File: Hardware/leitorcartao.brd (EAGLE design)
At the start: 34.5 x 56.7 mm, 154 parts, among them IC1 TL084, IC2 TL084, Q1 DMN3404, Q4 BC847ALT1SMD, Q5 BC847ALT1SMD, Q6 BC847ALT1SMD, Q7 BC847ALT1SMD, Q8 MMBT4403, Q9 MMBT4401, U1 SAMD20E14A-AUT, U3 TLV1117-50CDCYR, U4 MFRC52202HN1, U5 LP2985-33DBVR, X1 ANTENA 125kHz, X2 MIFARE ANTENA

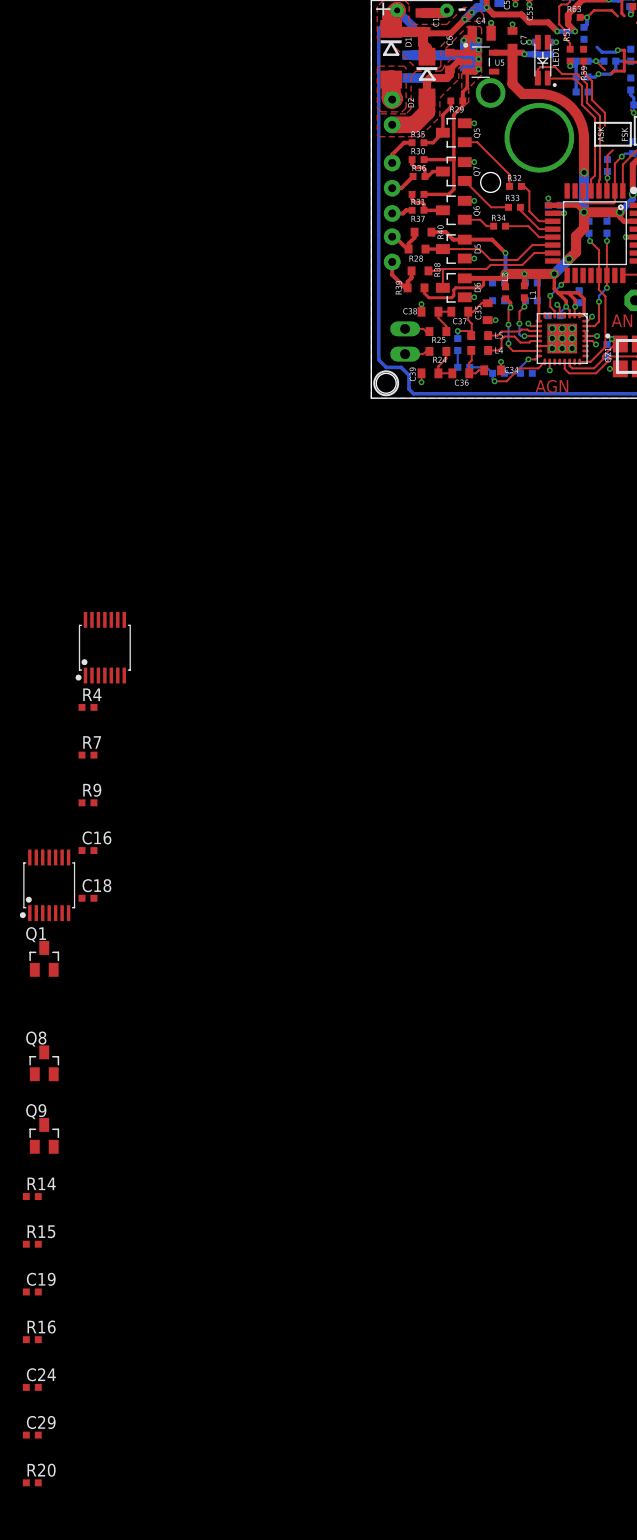
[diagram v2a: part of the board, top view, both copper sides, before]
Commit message: Finalização do esquema do RFID, falta valores de PSK e FSK.
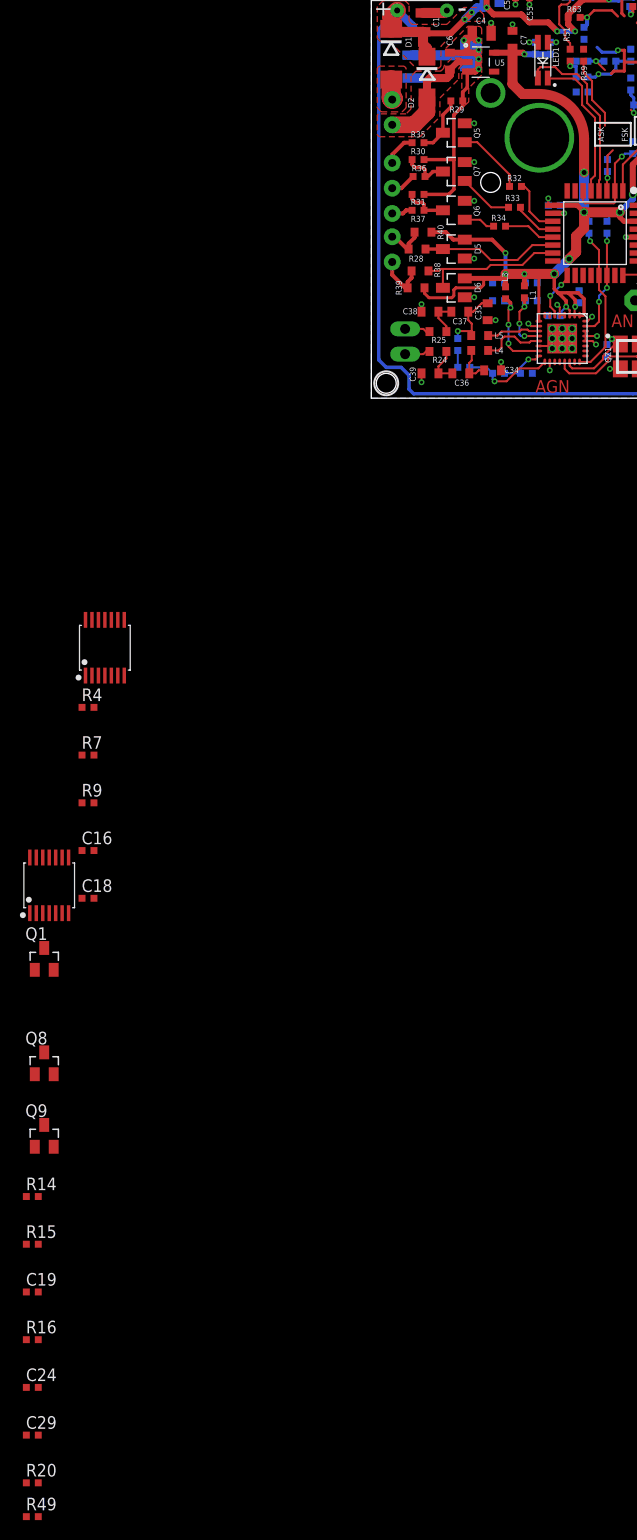
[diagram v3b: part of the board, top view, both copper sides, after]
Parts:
- added R49: F:P:5.1k, RFiD:R0402
- C24: value (none) -> F:C:100p
- C29, C48, C50: value (none) -> F:P:68p
- C47, C51: value (none) -> F:P:100p
- R14: value (none) -> 470k
- R15: value (none) -> 100
- R16, R51, R54: value (none) -> F:P:5.6k
- R20: value (none) -> C:P:270k
- R52, R55: value (none) -> F:P:5.1k
- R53, R56: value (none) -> F:P:270k
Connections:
- net GND: now also R49.1
- net N$29: now also R49.2
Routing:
- net N$28: track 4.20 -> 1.70 mm
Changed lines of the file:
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@@
 <attribute name="VALUE" x="23.805" y="42.165" size="1" layer="27" rot="R90"/>
 </element>
-<element name="R51" library="RFiD" package="R0402" value="" x="20" y="34.5" smashed="yes" rot="R270">
+<element name="R51" library="RFiD" package="R0402" value="F:P:5.6k" x="20" y="34.5" smashed="yes" rot="R270">
 <attribute name="CUSTOMER_PN" value="R/1k/5%/04" x="20" y="34.5" size="1.778" layer="27" rot="R270" display="off"/>
 <attribute name="NAME" x="19.335" y="37.335" size="0.6096" layer="25" font="vector" ratio="11" rot="R270"/>
 <attribute name="VALUE" x="18.095" y="35.135" size="1" layer="27" rot="R270"/>
 </element>
-<element name="R52" library="RFiD" package="R0402" value="" x="21.2" y="30.8" smashed="yes" rot="MR0">
+<element name="R52" library="RFiD" package="R0402" value="F:P:5.1k" x="21.2" y="30.8" smashed="yes" rot="MR0">
 <attribute name="CUSTOMER_PN" value="R/1k/5%/04" x="21.2" y="30.8" size="1.778" layer="28" rot="MR0" display="off"/>
 <attribute name="NAME" x="22.035" y="29.635" size="0.6096" layer="26" font="vector" ratio="11" rot="MR0"/>
 <attribute name="VALUE" x="21.835" y="28.895" size="1" layer="28" rot="MR0"/>
 </element>
-<element name="C47" library="RFiD" package="C0402" value="" x="21.2" y="33.9" smashed="yes" rot="MR0">
+<element name="C47" library="RFiD" package="C0402" value="F:P:100p" x="21.2" y="33.9" smashed="yes" rot="MR0">
 <attribute name="CUSTOMER_PN" value="C/1n/100V/C04" x="21.2" y="33.9" size="1.778" layer="28" rot="MR0" display="off"/>
 <attribute name="NAME" x="21.835" y="34.435" size="0.6096" layer="26" font="vector" ratio="11" rot="MR0"/>
 <attribute name="VALUE" x="21.835" y="31.995" size="1" layer="28" rot="MR0"/>
 </element>
-<element name="C48" library="RFiD" package="C0402" value="" x="21.2" y="32.3" smashed="yes" rot="MR0">
+<element name="C48" library="RFiD" package="C0402" value="F:P:68p" x="21.2" y="32.3" smashed="yes" rot="MR0">
 <attribute name="CUSTOMER_PN" value="C/1n/100V/C04" x="21.2" y="32.3" size="1.778" layer="28" rot="MR0" display="off"/>
 <attribute name="NAME" x="20.035" y="32.035" size="0.6096" layer="26" font="vector" ratio="11" rot="MR0"/>
 <attribute name="VALUE" x="21.835" y="30.395" size="1" layer="28" rot="MR0"/>
 </element>
-<element name="R53" library="RFiD" package="R0402" value="" x="24" y="33.9" smashed="yes" rot="MR180">
+<element name="R53" library="RFiD" package="R0402" value="F:P:270k" x="24" y="33.9" smashed="yes" rot="MR180">
 <attribute name="CUSTOMER_PN" value="R/1k/5%/04" x="24" y="33.9" size="1.778" layer="28" rot="MR180" display="off"/>
 <attribute name="NAME" x="23.165" y="33.265" size="0.6096" layer="26" font="vector" ratio="11" rot="MR180"/>
 <attribute name="VALUE" x="23.365" y="35.805" size="1" layer="28" rot="MR180"/>
 </element>
-<element name="R54" library="RFiD" package="R0402" value="" x="27.8" y="34.5" smashed="yes" rot="MR90">
+<element name="R54" library="RFiD" package="R0402" value="F:P:5.6k" x="27.8" y="34.5" smashed="yes" rot="MR90">
 <attribute name="CUSTOMER_PN" value="R/1k/5%/04" x="27.8" y="34.5" size="1.778" layer="28" rot="MR90" display="off"/>
 <attribute name="NAME" x="28.335" y="35.265" size="0.6096" layer="26" font="vector" ratio="11" rot="MR90"/>
@@
 <attribute name="VALUE" x="24.195" y="33.865" size="1" layer="28" rot="MR90"/>
 </element>
-<element name="R55" library="RFiD" package="R0402" value="" x="29.4" y="32.8" smashed="yes" rot="MR270">
+<element name="R55" library="RFiD" package="R0402" value="F:P:5.1k" x="29.4" y="32.8" smashed="yes" rot="MR270">
 <attribute name="CUSTOMER_PN" value="R/1k/5%/04" x="29.4" y="32.8" size="1.778" layer="28" rot="MR270" display="off"/>
 <attribute name="NAME" x="29.665" y="31.835" size="0.6096" layer="26" font="vector" ratio="11" rot="MR270"/>
 <attribute name="VALUE" x="31.305" y="33.435" size="1" layer="28" rot="MR270"/>
 </element>
-<element name="C50" library="RFiD" package="C0402" value="" x="27.8" y="31.6" smashed="yes" rot="MR90">
+<element name="C50" library="RFiD" package="C0402" value="F:P:68p" x="27.8" y="31.6" smashed="yes" rot="MR90">
 <attribute name="CUSTOMER_PN" value="C/1n/100V/C04" x="27.8" y="31.6" size="1.778" layer="28" rot="MR90" display="off"/>
 <attribute name="NAME" x="28.635" y="32.735" size="0.6096" layer="26" font="vector" ratio="11" rot="MR0"/>
 <attribute name="VALUE" x="25.895" y="30.965" size="1" layer="28" rot="MR90"/>
 </element>
-<element name="C51" library="RFiD" package="C0402" value="" x="26.1" y="31.6" smashed="yes" rot="MR90">
+<element name="C51" library="RFiD" package="C0402" value="F:P:100p" x="26.1" y="31.6" smashed="yes" rot="MR90">
 <attribute name="CUSTOMER_PN" value="C/1n/100V/C04" x="26.1" y="31.6" size="1.778" layer="28" rot="MR90" display="off"/>
 <attribute name="NAME" x="24.935" y="30.765" size="0.6096" layer="26" font="vector" ratio="11" rot="MR90"/>
 <attribute name="VALUE" x="24.195" y="30.965" size="1" layer="28" rot="MR90"/>
 </element>
-<element name="R56" library="RFiD" package="R0402" value="" x="27" y="29.5" smashed="yes" rot="MR0">
+<element name="R56" library="RFiD" package="R0402" value="F:P:270k" x="27" y="29.5" smashed="yes" rot="MR0">
 <attribute name="CUSTOMER_PN" value="R/1k/5%/04" x="27" y="29.5" size="1.778" layer="28" rot="MR0" display="off"/>
 <attribute name="NAME" x="28.765" y="30.335" size="0.6096" layer="26" font="vector" ratio="11" rot="MR270"/>
@@
 <element name="Q8" library="RFiD" package="SOT23" value="MMBT4403" x="-32.9" y="-66.9"/>
 <element name="Q9" library="RFiD" package="SOT23" value="MMBT4401" x="-32.9" y="-74.2"/>
-<element name="R14" library="RFiD" package="R0402" value="" x="-34.1" y="-80.3">
+<element name="R14" library="RFiD" package="R0402" value="470k" x="-34.1" y="-80.3">
 <attribute name="CUSTOMER_PN" value="R/1M/5%/04" x="-34.1" y="-80.3" size="1.778" layer="27" display="off"/>
 </element>
-<element name="R15" library="RFiD" package="R0402" value="" x="-34.1" y="-85.1">
+<element name="R15" library="RFiD" package="R0402" value="100" x="-34.1" y="-85.1">
 <attribute name="CUSTOMER_PN" value="R/1M/5%/04" x="-34.1" y="-85.1" size="1.778" layer="27" display="off"/>
 </element>
@@
 <attribute name="CUSTOMER_PN" value="C/1n/100V/C04" x="-34.1" y="-89.9" size="1.778" layer="27" display="off"/>
 </element>
-<element name="R16" library="RFiD" package="R0402" value="" x="-34.1" y="-94.7">
+<element name="R16" library="RFiD" package="R0402" value="F:P:5.6k" x="-34.1" y="-94.7">
 <attribute name="CUSTOMER_PN" value="R/1k/5%/04" x="-34.1" y="-94.7" size="1.778" layer="27" display="off"/>
 </element>
-<element name="C24" library="RFiD" package="C0402" value="" x="-34.1" y="-99.5">
+<element name="C24" library="RFiD" package="C0402" value="F:C:100p" x="-34.1" y="-99.5">
 <attribute name="CUSTOMER_PN" value="C/1n/100V/C04" x="-34.1" y="-99.5" size="1.778" layer="27" display="off"/>
 </element>
-<element name="C29" library="RFiD" package="C0402" value="" x="-34.1" y="-104.3">
+<element name="C29" library="RFiD" package="C0402" value="F:P:68p" x="-34.1" y="-104.3">
 <attribute name="CUSTOMER_PN" value="C/1n/100V/C04" x="-34.1" y="-104.3" size="1.778" layer="27" display="off"/>
 </element>
-<element name="R20" library="RFiD" package="R0402" value="" x="-34.1" y="-109.1">
+<element name="R20" library="RFiD" package="R0402" value="C:P:270k" x="-34.1" y="-109.1">
 <attribute name="CUSTOMER_PN" value="R/1k/5%/04" x="-34.1" y="-109.1" size="1.778" layer="27" display="off"/>
+</element>
+<element name="R49" library="RFiD" package="R0402" value="F:P:5.1k" x="-34.1" y="-112.5">
+<attribute name="CUSTOMER_PN" value="R/1k/5%/04" x="-34.1" y="-112.5" size="1.778" layer="27" display="off"/>
 </element>
 </elements>
@@
 <contactref element="IC1" pad="11"/>
 <contactref element="IC2" pad="11"/>
+<contactref element="R49" pad="1"/>
+<wire x1="-32.9" y1="-65.8" x2="-34.7" y2="-112.5" width="0" layer="19" extent="1-1"/>
 <wire x1="-31.95" y1="-57.5" x2="-32.9" y2="-65.8" width="0" layer="19" extent="1-1"/>
 <wire x1="-32.4" y1="-46.2" x2="-31.95" y2="-57.5" width="0" layer="19" extent="1-1"/>
@@
 <wire x1="20" y1="35.7" x2="20" y2="35.1" width="0.2032" layer="1"/>
 </signal>
-<signal name="N$70">
-<contactref element="R51" pad="2"/>
-<contactref element="C47" pad="2"/>
-<contactref element="R52" pad="2"/>
-<contactref element="C48" pad="2"/>
-<wire x1="20.6" y1="30.8" x2="20.6" y2="32.3" width="0.3048" layer="16"/>
-<wire x1="20.6" y1="32.3" x2="20.6" y2="33.4" width="0.3048" layer="16"/>
-<wire x1="20.6" y1="33.4" x2="20.6" y2="33.9" width="0.3048" layer="16"/>
-<via x="20" y="33.4" extent="1-16" drill="0.3"/>
-<wire x1="20" y1="33.4" x2="20" y2="33.9" width="0.2032" layer="1"/>
-<wire x1="20.6" y1="33.4" x2="20" y2="33.4" width="0.3048" layer="16"/>
-</signal>
 <signal name="N$71">
 <contactref element="C48" pad="1"/>
@@
 <contactref element="C24" pad="2"/>
 <contactref element="R16" pad="2"/>
+<contactref element="R49" pad="2"/>
+<wire x1="-33.5" y1="-104.3" x2="-33.5" y2="-112.5" width="0" layer="19" extent="1-1"/>
 <wire x1="-33.5" y1="-99.5" x2="-33.5" y2="-104.3" width="0" layer="19" extent="1-1"/>
 <wire x1="-33.5" y1="-94.7" x2="-33.5" y2="-99.5" width="0" layer="19" extent="1-1"/>
@@
 <wire x1="-24.85" y1="-22.3" x2="17.6" y2="40.4" width="0" layer="19" extent="1-16"/>
 </signal>
+<signal name="N$28">
+<contactref element="R51" pad="2"/>
+<contactref element="C47" pad="2"/>
+<contactref element="R52" pad="2"/>
+<contactref element="C48" pad="2"/>
+<wire x1="20.6" y1="32.3" x2="20.6" y2="33.4" width="0.3048" layer="16"/>
+<via x="20" y="33.4" extent="1-16" drill="0.3"/>
+<wire x1="20.6" y1="33.4" x2="20" y2="33.4" width="0.3048" layer="16"/>
+<wire x1="20.6" y1="33.4" x2="20.6" y2="33.9" width="0" layer="19" extent="16-16"/>
+<wire x1="20" y1="33.9" x2="20" y2="33.4" width="0" layer="19" extent="1-1"/>
+<wire x1="20.6" y1="30.8" x2="20.6" y2="32.3" width="0" layer="19" extent="16-16"/>
+</signal>
 </signals>

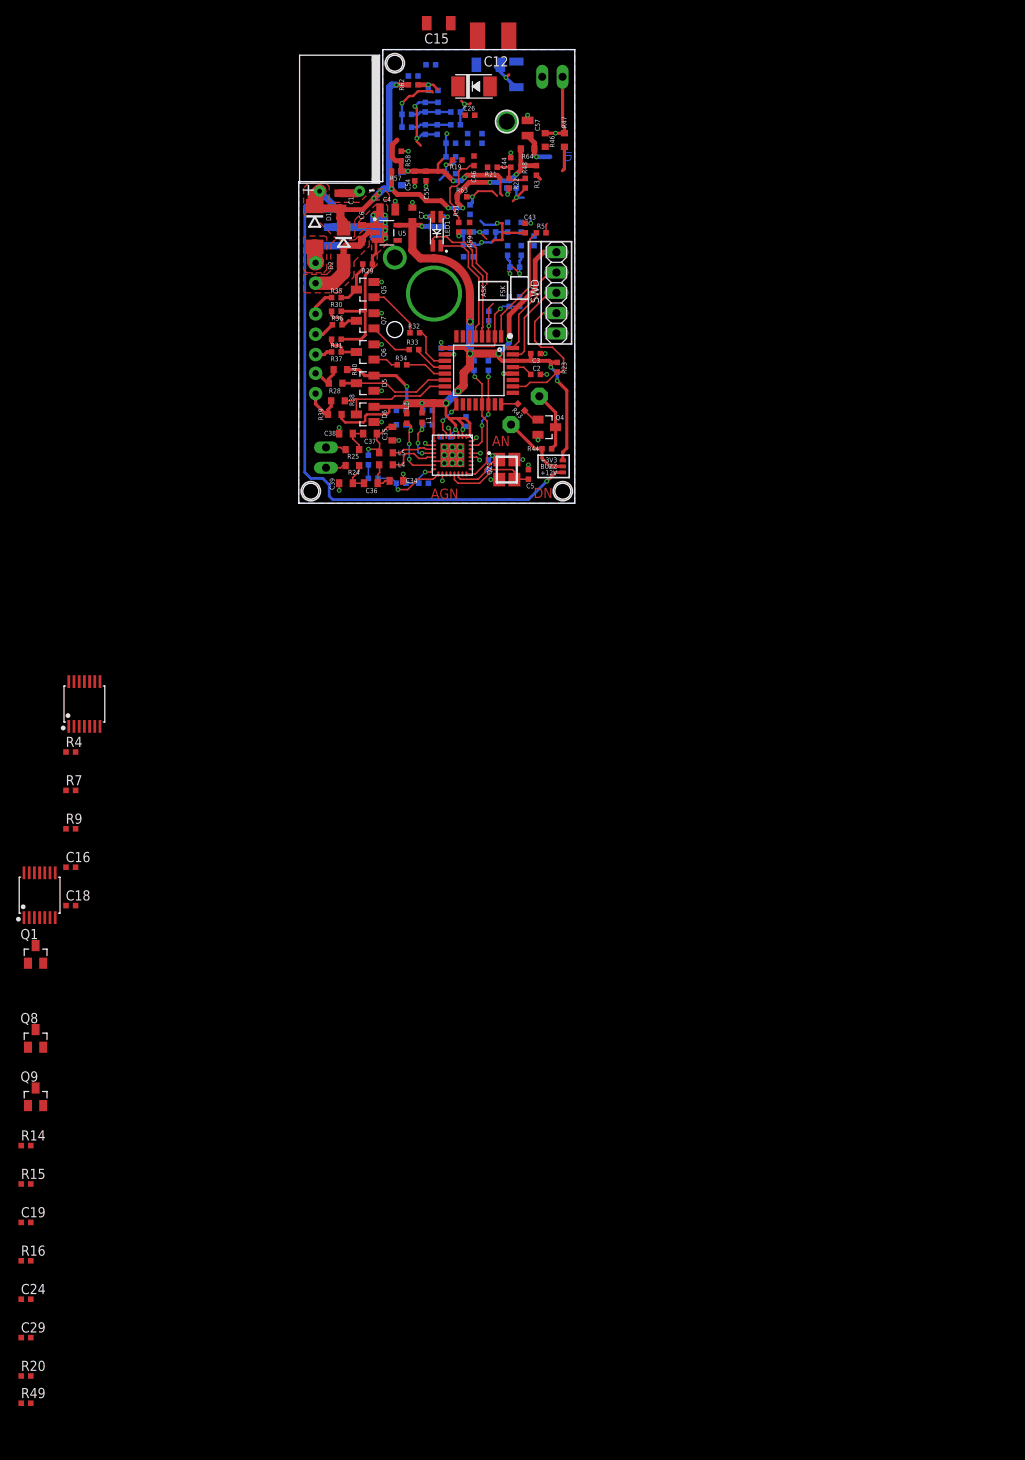
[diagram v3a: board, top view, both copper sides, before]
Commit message: Correção de conexões dos OpAmps.
Alteração de valores do ASK.
Correções na topologia do PSK.
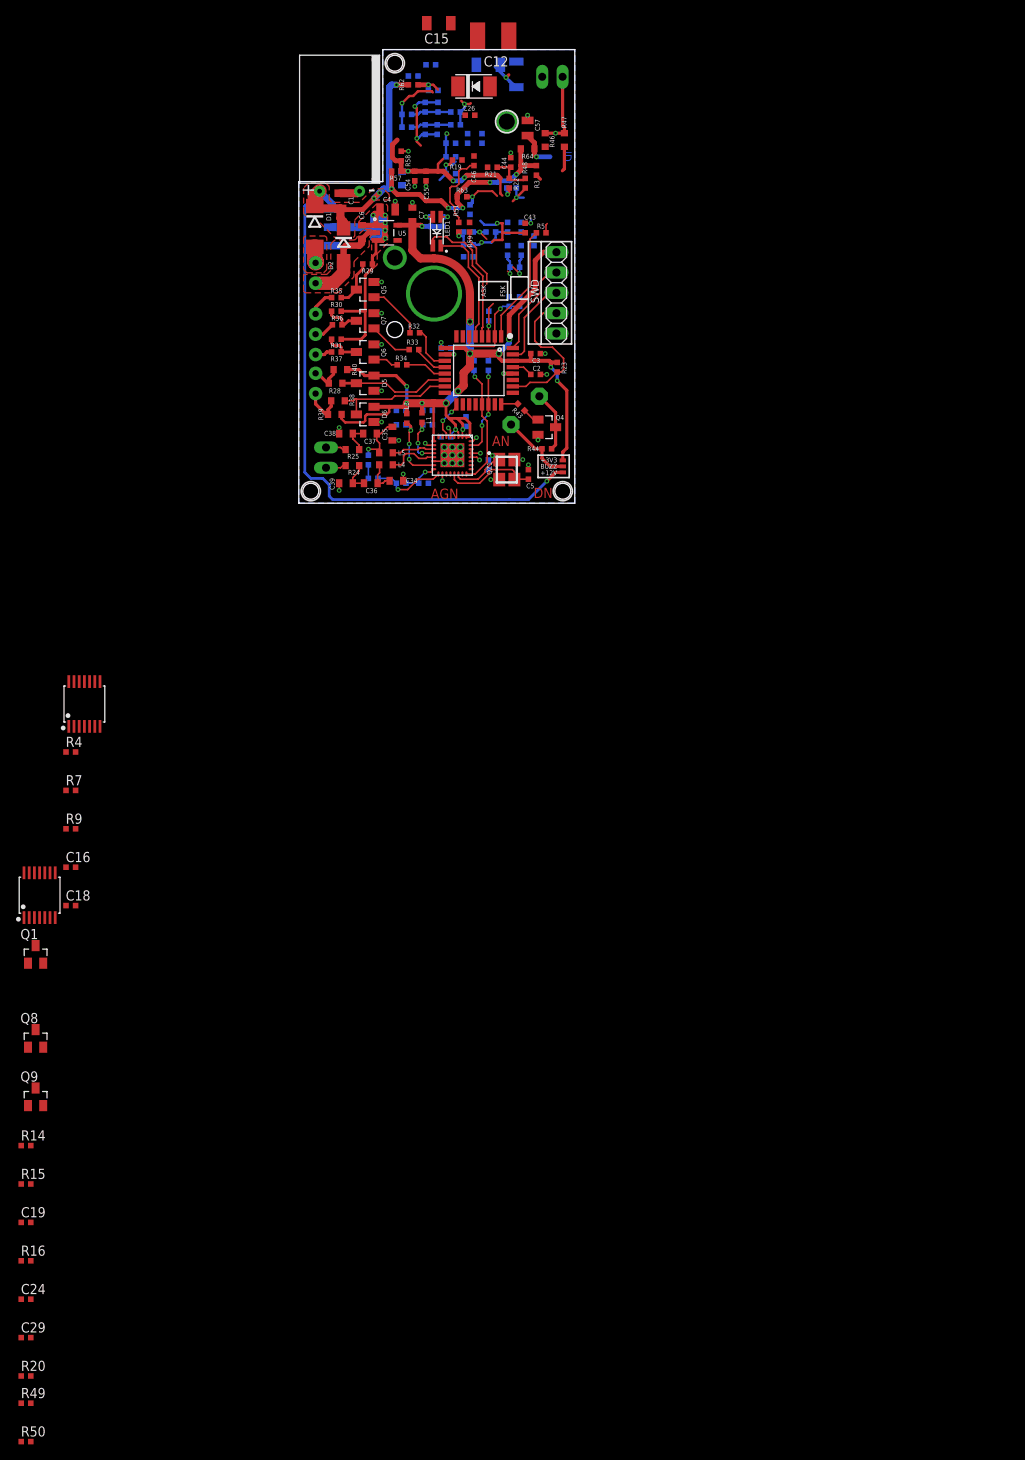
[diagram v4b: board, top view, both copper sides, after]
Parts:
- added R50: 100k, RFiD:R0402
- C25, C44: value 2.2n -> 4.7n
- C26, C28: value 0.1u -> 220n
- C27, C45: value 100p -> 68p
- R17, R21: value 7.5k -> 4.7k
- R18, R22: value 12k -> 13k
- R19, R48: value 150k -> 91k
- X1: value ANTENA 125kHz -> ANTENA
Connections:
- new net N$58: IC1.3, R50.1
- net GND: no longer R49.1, R52.1, R55.1
- net N$14: now also R50.2; no longer IC1.3
- net N$27: now also IC1.9; no longer IC1.10
- net N$63: now also R48.1; no longer R48.2
- net N$64: now also IC1.13; no longer IC1.12
- net N$72: now also IC2.6; no longer IC2.5
- net N$90: now also R48.2; no longer R48.1
- net V+: now also IC1.10, IC1.12, IC2.5, R49.1, R52.1, R55.1; no longer IC1.13, IC1.9, IC2.6
